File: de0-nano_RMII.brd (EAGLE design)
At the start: 75.2 x 49 mm, 49 parts, among them IC2 AD5683, U1 DP83848, X1 1-227161-2

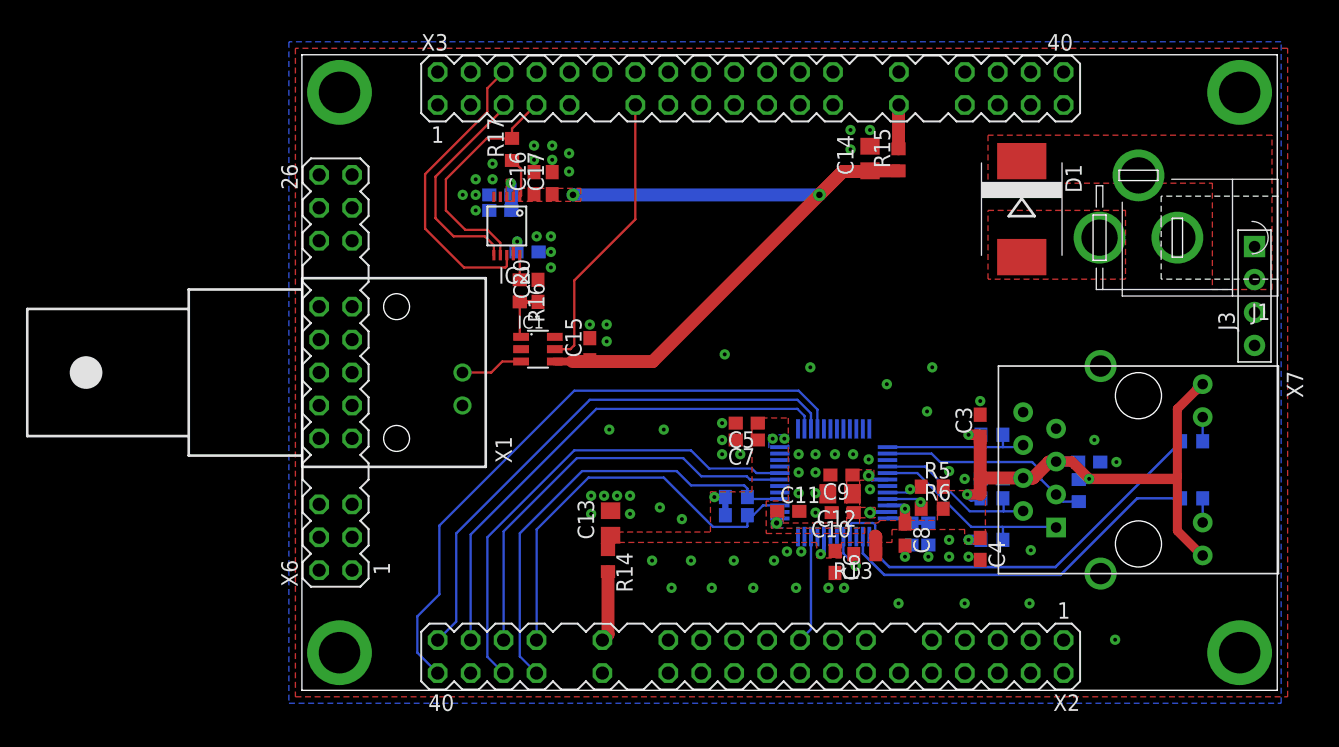
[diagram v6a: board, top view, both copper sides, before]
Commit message: added protection diodes at the input, and separate crystal oscillator
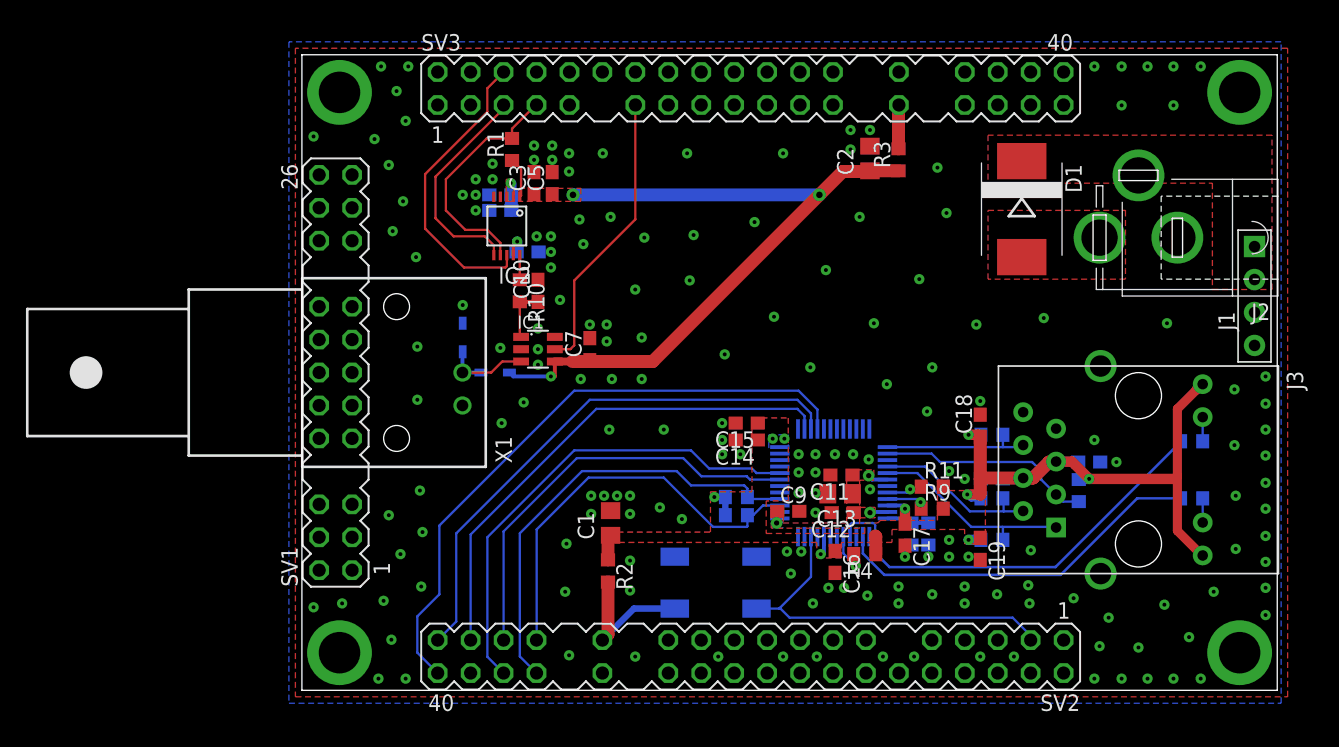
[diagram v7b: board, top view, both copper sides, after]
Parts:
- removed X7: (no value), seeed_connector:RJ45
- added D2, D3: (no value), zetex:SOD323
- added J2: (no value), con-jack:SPC4078
- added SV2: (no value), con-lstb:MA20-2_ALT
- C1, C2: value 100nF -> 10uF; device resistor:C0603 -> resistor:C0805
- C12, C14: value 10uF -> 100nF; device resistor:C0805 -> resistor:C0603
- J1: device con-jack:SPC4078 -> seeed_connector:4P-65/35MIL
- J3: device seeed_connector:4P-65/35MIL -> seeed_connector:RJ45
- R1: value 330R -> 4k7
- R11, R9: value 51R -> 2k 1%
- R13: value 4k7 -> 51R
- R14, R15: value BLM -> 51R
- R16: value 51R -> 330R
- R17: value 4k7 -> 330R
- R2: value 330R -> BLM
- R3: value 2k 1% -> BLM
- R4: value 2k 1% -> 4k7
- R5: value 2k 1% -> 12k 1%
- R6: value 2k 1% -> 8k2 1%
- R7: value 12k 1% -> 2k 1%
- R8: value 8k2 1% -> 2k 1%
- X2: value (none) -> CRYSTALS-GND-LID12SMX-B-4-PAD; device con-lstb:MA20-2_ALT -> IQD-Frequency-Products:7.5X5-4-PAD
- moved R17 58.9 mm to (68.6, 14.8), flipped to the bottom, turned to 180 degrees
- moved R1 57.0 mm to (16.2, 41.7), flipped to the top, turned to 90 degrees
- moved R16 53.1 mm to (68.6, 19.2), flipped to the bottom, turned to 0 degrees
- moved C21 46.2 mm to (60.7, 17.6)
- moved C4 46.0 mm to (15.3, 38.2), flipped to the bottom, turned to 0 degrees
- moved R2 45.3 mm to (23.6, 9.20), flipped to the top, turned to 270 degrees
- moved C19 45.3 mm to (52.3, 10.9), flipped to the top, turned to 270 degrees
- moved C18 41.1 mm to (52.3, 20.4), flipped to the top, turned to 90 degrees
- moved C3 39.2 mm to (17.9, 39.1)
- moved C17 38.4 mm to (46.5, 12.0), turned to 270 degrees
- moved R10 38.1 mm to (16.8, 30.8), flipped to the top, turned to 270 degrees
- moved C20 37.9 mm to (53.2, 16.3), flipped to the bottom, turned to 0 degrees
- moved C6 37.4 mm to (15.3, 37.0), flipped to the bottom, turned to 0 degrees
- moved C16 37.3 mm to (41.1, 9.90), turned to 270 degrees
- moved C8 36.4 mm to (17.4, 33.8), flipped to the bottom, turned to 180 degrees
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- renumbered U1 to IC3, X3 to SV3, X6 to SV1
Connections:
- removed net N$7: R14.2, X2.29
- new net RAW_3V3: R2.2, SV2.29, X2.4
- net 3V3: now also C14.1, C15.1, C16.1, C17.1, C18.1, C19.1, C20.1, C21.1, J3.G+, J3.P4, J3.P5, J3.Y+, R11.2, R14.2, R15.1, R2.1, R4.1, R7.2, R8.2, R9.2; no longer C13.1, C2.1, C3.1, C4.1, C5.1, C6.1, C7.1, C8.1, R10.2, R11.1, R14.1, R3.2, R4.2, R5.2, R6.2, R9.1, X7.G+, X7.P4, X7.P5, X7.Y+
- net 3V3_A: now also C2.1, C3.1, C5.1, C7.1, D2.1, R1.1, R3.1; no longer C14.1, C15.1, C16.1, C17.1, R15.1, R17.1
- net CRS_DV: now also R8.1, SV2.34; no longer R4.1, X2.34
- net DAC_NCS: now also R1.2; no longer R17.2
- net GND: now also D3.2, J1.3, J1.4, J2.1, J2.2, J3.GND, J3.NC, J3.SHIELD0, J3.SHIELD1, R5.2, R6.2, SV2.12, SV2.30, X2.2; no longer J1.1, J1.2, J3.3, J3.4, R7.2, R8.2, X2.12, X2.30, X7.GND, X7.NC, X7.SHIELD0, X7.SHIELD1
- net LED_ACT: now also R17.1; no longer R2.1
- net LED_LINK: now also R16.2; no longer R1.2
- net N$1: now also R3.2; no longer R15.2
- net N$13: now also C8.1; no longer C21.1
- net N$3: now also R9.1; no longer R6.1
- net N$4: now also J3.Y-, R16.1; no longer R1.1, X7.Y-
- net N$5: now also R11.1; no longer R5.1
- net N$6: now also J3.G-, R17.2; no longer R2.2, X7.G-
- net N$8: now also R10.1; no longer R16.1
- net N$9: now also R5.1, R6.1; no longer R7.1, R8.1
- net OSCIN: now also SV2.3, X2.3; no longer X2.17
- net PFB: now also C13.1; no longer C10.1
- net RST_N: now also R4.2; no longer R13.2
- net RX+: now also J3.RD+, R13.2; no longer R9.2, X7.RD+
- net RX-: now also J3.RD-, R12.1; no longer R10.1, X7.RD-
- net RXD_0: now also SV2.35; no longer X2.35
- net RXD_1: now also SV2.36; no longer X2.36
- net RX_DV: now also R7.1, SV2.33; no longer R3.1, X2.33
- net SIG_IN: now also D2.2, D3.1
- net THR_LVL: now also C10.1, R10.2; no longer C20.1, R16.2
- net TX+: now also J3.TD+, R15.2; no longer R11.2, X7.TD+
- net TX-: now also J3.TD-, R14.1; no longer R12.1, X7.TD-
- net TXD_0: now also SV2.39; no longer X2.39
- net TXD_1: now also SV2.40; no longer X2.40
- net TX_EN: now also SV2.37; no longer X2.37
- net VCC_SYS: now also J1.1, J1.2; no longer J3.1, J3.2
- net VLOGIC: now also C4.1, C6.1; no longer C18.1, C19.1
- net V_RAW: now also J2.3; no longer J1.3
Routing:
- net OSCIN: track 8.33 -> 28.9 mm
- net RAW_3V3: track 0.00 -> 11.2 mm
- net N$7: track 5.46 -> 0.00 mm
- net SIG_IN: track 4.87 -> 7.91 mm
- net 3V3_A: track 58.0 -> 60.2 mm, vias 2 -> 3
- net 3V3: track 54.0 -> 54.8 mm

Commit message: gerber generated
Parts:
- C13: value 10uF -> 100nF; device resistor:C0805 -> resistor:C0603
- C7: value 100nF -> 10uF; device resistor:C0603 -> resistor:C0805
- IC1: value (none) -> DP83848; device linear-technology:TSOT23-6 -> national-semiconductor:LQFP48
- IC2: value AD5683 -> (none); device analog-devices:SO10 -> linear-technology:TSOT23-6
- IC3: value DP83848 -> AD5683; device national-semiconductor:LQFP48 -> analog-devices:SO10
- J1: device seeed_connector:4P-65/35MIL -> con-jack:SPC4078
- J2: device con-jack:SPC4078 -> seeed_connector:4P-65/35MIL
- R10: value 51R -> 2k 1%
- R11: value 2k 1% -> 51R
- X1: value 1-227161-2 -> CRYSTALS-GND-LID12SMX-B-4-PAD; device con-coax:AMP_227161 -> IQD-Frequency-Products:7.5X5-4-PAD
- X2: value CRYSTALS-GND-LID12SMX-B-4-PAD -> 1-227161-2; device IQD-Frequency-Products:7.5X5-4-PAD -> con-coax:AMP_227161
- moved C21 44.5 mm to (18.2, 30.8), flipped to the top, turned to 90 degrees
- moved R15 41.2 mm to (16.8, 30.8), flipped to the top, turned to 270 degrees
- moved C17 40.0 mm to (15.3, 37.0), flipped to the bottom, turned to 0 degrees
- moved C20 39.8 mm to (17.4, 33.8), turned to 180 degrees
- moved C16 36.4 mm to (19.3, 39.1), turned to 90 degrees
- moved C12 36.0 mm to (15.3, 38.2), flipped to the bottom, turned to 0 degrees
- moved C6 35.2 mm to (41.7, 13.7), flipped to the top, turned to 180 degrees
- moved R10 35.2 mm to (48.6, 15.7), turned to 0 degrees
- moved C4 34.0 mm to (41.6, 16.6), flipped to the top, turned to 180 degrees
- moved C11 32.7 mm to (17.9, 39.1), turned to 90 degrees
- moved IC3 32.0 mm to (15.8, 35.8), flipped to the top, turned to 180 degrees
- moved C3 32.0 mm to (37.5, 13.8), turned to 0 degrees
- moved C10 31.0 mm to (41.1, 9.90), turned to 270 degrees
- moved X1 29.5 mm to (31.9, 8.30), flipped to the bottom, turned to 180 degrees
- moved X2 29.5 mm to (7.30, 24.5), flipped to the top, turned to 90 degrees
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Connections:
- net 3V3: now also C10.1, C13.1, C8.1, C9.1, IC1.22, IC1.32, IC1.48, R10.2, R12.1, R13.2, R14.1; no longer C16.1, C17.1, C20.1, C21.1, IC3.22, IC3.32, IC3.48, R12.2, R13.1, R14.2, R15.1
- net 3V3_A: now also C11.1, C16.1, IC2.4, IC3.1; no longer C3.1, C7.1, IC1.4, IC2.1
- net COM_OUT: now also IC2.5; no longer IC1.5
- net CRS_DV: now also IC1.40; no longer IC3.40
- net DAC_CLK: now also IC3.6; no longer IC2.6
- net DAC_NCS: now also IC3.7; no longer IC2.7
- net DAC_SDI: now also IC3.8; no longer IC2.8
- net GND: now also IC1.15, IC1.19, IC1.35, IC1.36, IC1.47, IC2.2, IC2.6, IC3.4, IC3.5, J1.1, J1.2, J2.3, J2.4; no longer IC1.2, IC1.6, IC2.4, IC2.5, IC3.15, IC3.19, IC3.35, IC3.36, IC3.47, J1.3, J1.4, J2.1, J2.2
- net LED_ACT: now also IC1.26; no longer IC3.26
- net LED_LINK: now also IC1.28; no longer IC3.28
- net MDC: now also IC1.31; no longer IC3.31
- net MDIO: now also IC1.30; no longer IC3.30
- net N$13: now also C20.1, IC3.9; no longer C8.1, IC2.9
- net N$3: now also IC1.21; no longer IC3.21
- net N$5: now also IC1.20, R10.1; no longer IC3.20, R11.1
- net N$8: now also IC3.10, R15.1; no longer IC2.10, R10.1
- net N$9: now also IC1.24; no longer IC3.24
- net OSCIN: now also IC1.34, X1.3; no longer IC3.34, X2.3
- net PFB: now also C3.1, C4.1, C6.1, C7.1, IC1.18, IC1.23, IC1.37; no longer C11.1, C12.1, C13.1, C9.1, IC3.18, IC3.23, IC3.37
- net RAW_3V3: now also X1.4; no longer X2.4
- net RST_N: now also IC1.29; no longer IC3.29
- net RX+: now also IC1.14, R12.2; no longer IC3.14, R13.2
- net RX-: now also IC1.13, R11.1; no longer IC3.13, R12.1
- net RXD_0: now also IC1.43; no longer IC3.43
- net RXD_1: now also IC1.44; no longer IC3.44
- net RX_DV: now also IC1.39; no longer IC3.39
- net SIG_IN: now also IC2.3, X2.1; no longer IC1.3, X1.1
- net THR_LVL: now also C21.1, IC2.1, R15.2; no longer C10.1, IC1.1, R10.2
- net TX+: now also IC1.17, R14.2; no longer IC3.17, R15.2
- net TX-: now also IC1.16, R13.1; no longer IC3.16, R14.1
- net TXD_0: now also IC1.3; no longer IC3.3
- net TXD_1: now also IC1.4; no longer IC3.4
- net TX_EN: now also IC1.2; no longer IC3.2
- net VCC_SYS: now also J2.1, J2.2; no longer J1.1, J1.2
- net VLOGIC: now also C12.1, C17.1, IC3.2, IC3.3; no longer C4.1, C6.1, IC2.2, IC2.3
- net V_RAW: now also J1.3; no longer J2.3
